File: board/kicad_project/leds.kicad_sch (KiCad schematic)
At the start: 32 parts, among them U4 74LS07, U5 74LS07

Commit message: Initial board design
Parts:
- C20, C21: footprint Capacitor_SMD:C_0603_1608Metric -> Capacitor_SMD:C_0805_2012Metric
- R22: renamed from R21; footprint Resistor_SMD:R_0603_1608Metric -> Resistor_SMD:R_0805_2012Metric
- R23: renamed from R22; footprint Resistor_SMD:R_0603_1608Metric -> Resistor_SMD:R_0805_2012Metric
- R24: renamed from R23; footprint Resistor_SMD:R_0603_1608Metric -> Resistor_SMD:R_0805_2012Metric
- R25: renamed from R24; footprint Resistor_SMD:R_0603_1608Metric -> Resistor_SMD:R_0805_2012Metric
- R26: renamed from R25; footprint Resistor_SMD:R_0603_1608Metric -> Resistor_SMD:R_0805_2012Metric
- R27: renamed from R26; footprint Resistor_SMD:R_0603_1608Metric -> Resistor_SMD:R_0805_2012Metric
- R28: renamed from R27; footprint Resistor_SMD:R_0603_1608Metric -> Resistor_SMD:R_0805_2012Metric
- R29: renamed from R28; footprint Resistor_SMD:R_0603_1608Metric -> Resistor_SMD:R_0805_2012Metric
- R30: renamed from R29; footprint Resistor_SMD:R_0603_1608Metric -> Resistor_SMD:R_0805_2012Metric
- R31: renamed from R30; footprint Resistor_SMD:R_0603_1608Metric -> Resistor_SMD:R_0805_2012Metric
- R32: renamed from R31; footprint Resistor_SMD:R_0603_1608Metric -> Resistor_SMD:R_0805_2012Metric
- R33: renamed from R32; footprint Resistor_SMD:R_0603_1608Metric -> Resistor_SMD:R_0805_2012Metric
- R34: renamed from R33; footprint Resistor_SMD:R_0603_1608Metric -> Resistor_SMD:R_0805_2012Metric
- R35: renamed from R34; footprint Resistor_SMD:R_0603_1608Metric -> Resistor_SMD:R_0805_2012Metric
- renumbered U4 to U3, U5 to U4
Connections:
- net AVR_PA0: now also U3.9; no longer U3.1
- net AVR_PA1: now also U3.11; no longer U3.3
- net AVR_PA2: now also U3.13; no longer U3.5
- net AVR_PA3: now also U4.1; no longer U3.9
- net AVR_PA4: now also U4.3; no longer U3.11
- net AVR_PA5: now also U4.5; no longer U3.13
- net AVR_PA6: now also U4.9; no longer U4.1
- net AVR_PA7: now also U4.11; no longer U4.3
- net AVR_PB0: now also U3.5; no longer U4.5
- net AVR_PB1: now also U3.3; no longer U4.9
- net AVR_PB2: now also U4.13; no longer U4.11
- net AVR_PB3: now also U3.1; no longer U4.13
- net at R25.1: now also U4.2; no longer U3.8
- net at R24.1: now also U3.12; no longer U3.6
- net at R28.1: now also U4.8; no longer U4.2
- net at R22.1: now also U3.8; no longer U3.2
- net at R33.1: now also U3.2; no longer U4.12
- net at R26.1: now also U4.4; no longer U3.10
- net at R30.1: now also U3.6; no longer U4.6
- net at R29.1: now also U4.10; no longer U4.4
- net at R23.1: now also U3.10; no longer U3.4
- net at R32.1: now also U4.12; no longer U4.10
- net at R27.1: now also U4.6; no longer U3.12
- net at R31.1: now also U3.4; no longer U4.8
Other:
- moved on the sheet: U3A, U3B, U3C, U3D, U3E, U3F, U4A, U4B, U4C, U4D, U4E, U4F

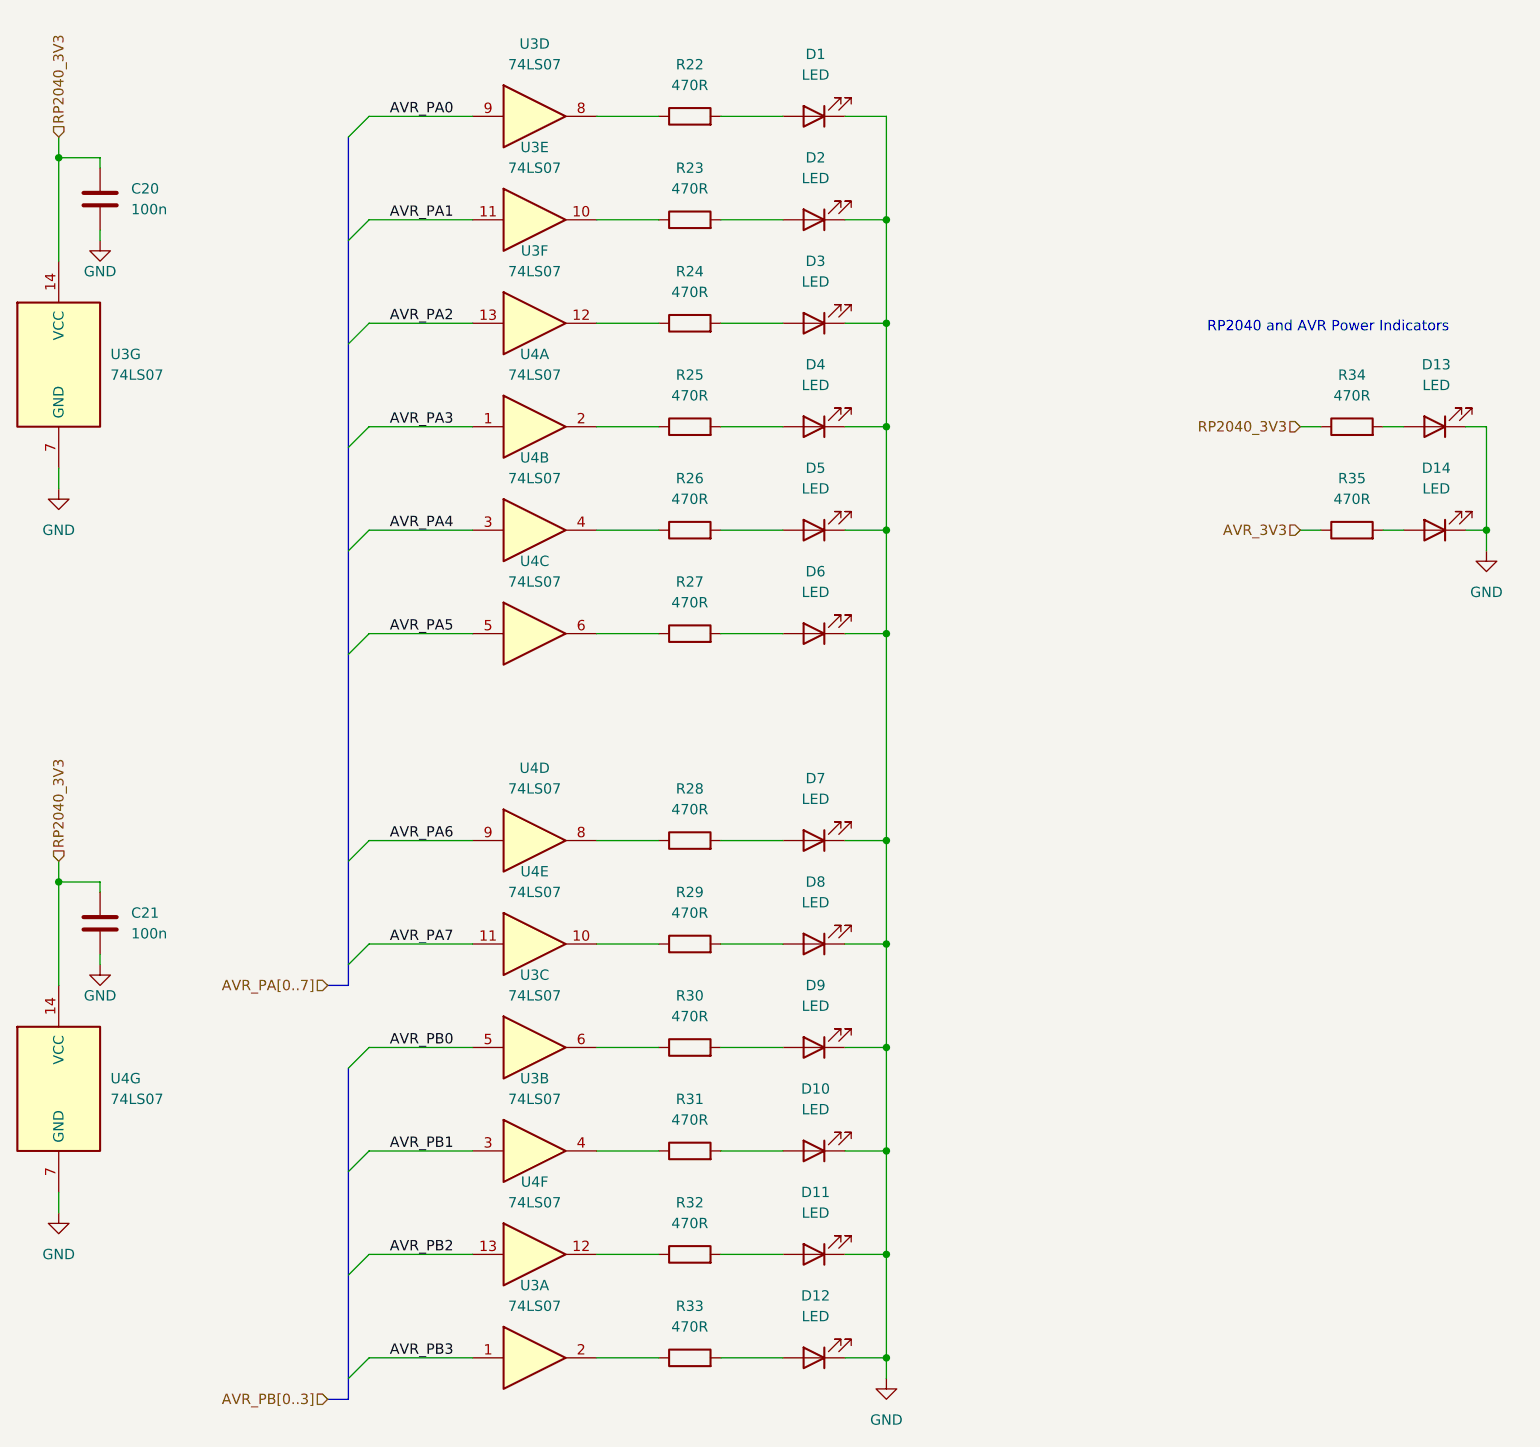
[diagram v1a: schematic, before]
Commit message: Added lcsc part numbers
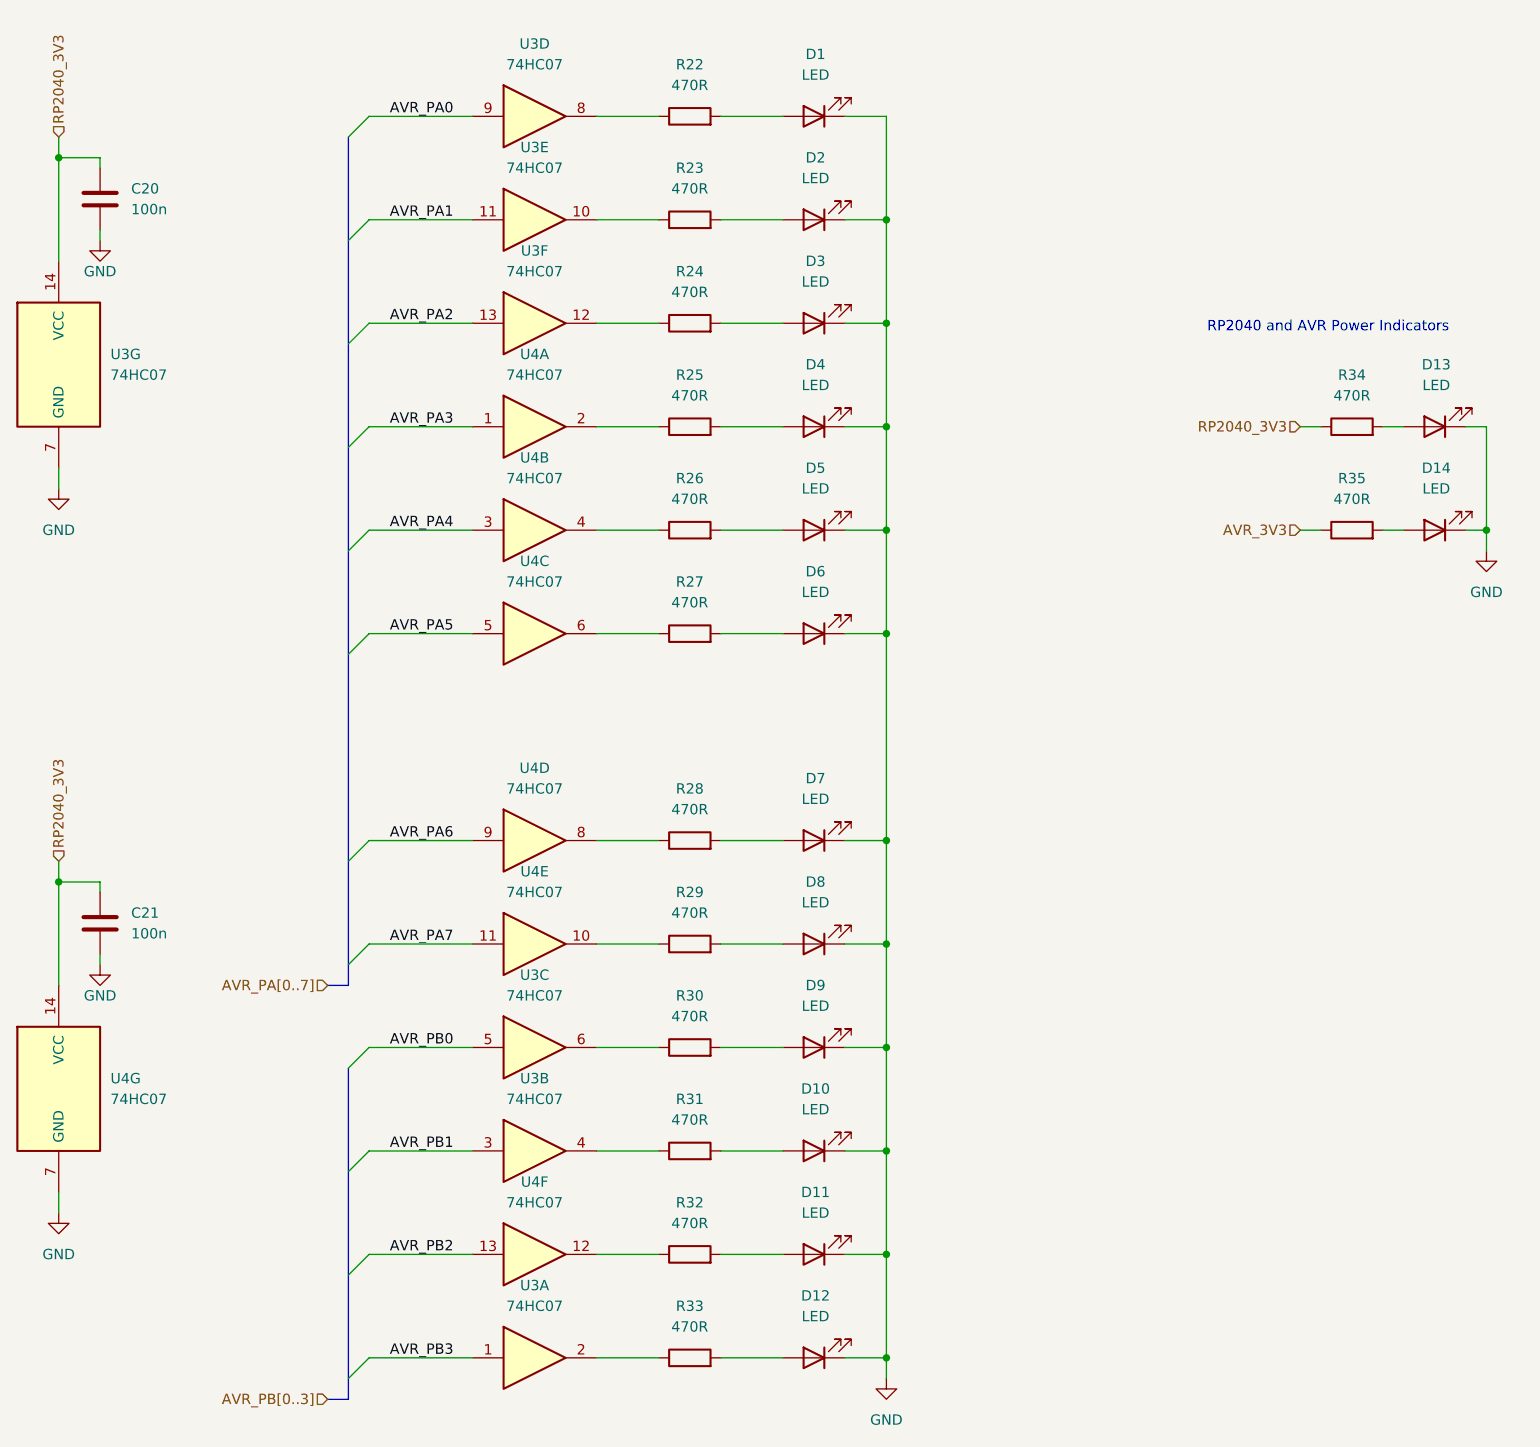
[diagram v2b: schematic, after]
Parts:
- C20, C21: LCSC Part (none) -> C49678
- D1, D10, D11, D12, D13, D14, D2, D3, D4, D5, D6, D7, D8, D9: LCSC Part (none) -> C72041
- R22, R23, R24, R25, R26, R27, R28, R29, R30, R31, R32, R33, R34, R35: LCSC Part (none) -> C17710
- U3, U4: value 74LS07 -> 74HC07; LCSC Part (none) -> C512771
